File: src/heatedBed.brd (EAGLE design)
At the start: 100 x 100 mm, 20 parts, among them P2 LONG_PAD

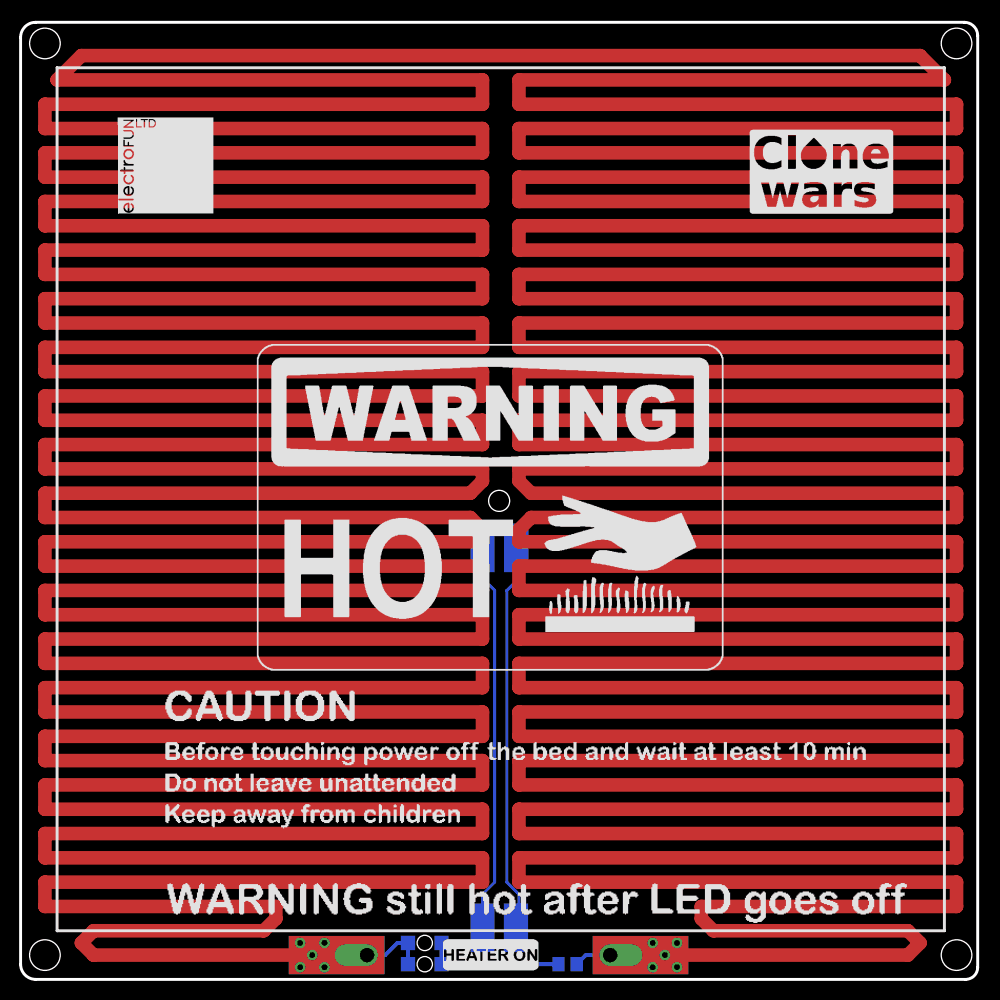
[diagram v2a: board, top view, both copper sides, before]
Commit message: Added board dimensions and modified drill sizes.
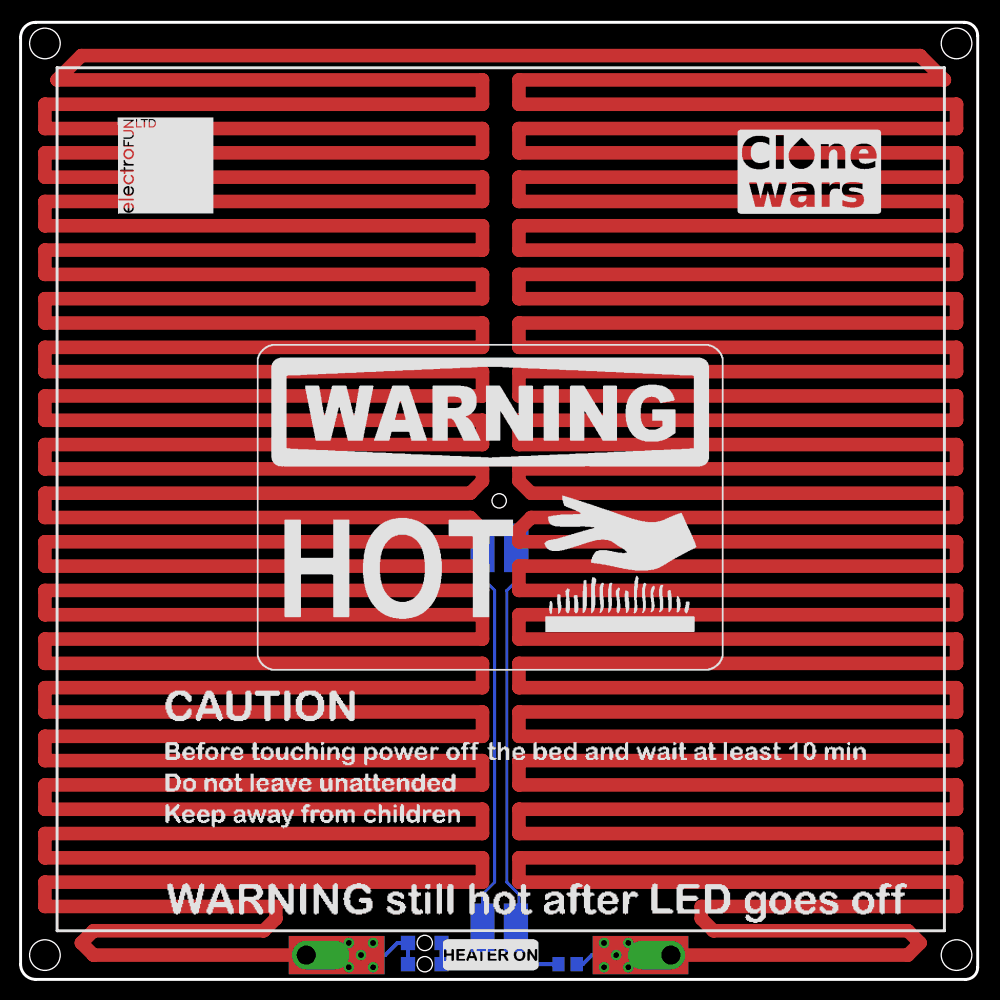
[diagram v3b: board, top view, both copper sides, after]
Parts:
- moved U$11 2.54 mm to (88.9, 58.7)
- moved U$3 1.27 mm to (74.9, 80.0)
- turned P2 to 0 degrees
- turned U$2 to 180 degrees
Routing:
- net P1: track 3547.0 -> 3543.8 mm
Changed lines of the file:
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@@
 <layer number="23" name="tOrigins" color="15" fill="1" visible="yes" active="yes"/>
 <layer number="24" name="bOrigins" color="15" fill="1" visible="yes" active="yes"/>
-<layer number="25" name="tNames" color="7" fill="1" visible="no" active="yes"/>
+<layer number="25" name="tNames" color="7" fill="1" visible="yes" active="yes"/>
 <layer number="26" name="bNames" color="7" fill="1" visible="yes" active="yes"/>
 <layer number="27" name="tValues" color="7" fill="1" visible="no" active="yes"/>
@@
 <layer number="45" name="Holes" color="7" fill="1" visible="yes" active="yes"/>
 <layer number="46" name="Milling" color="3" fill="1" visible="no" active="yes"/>
-<layer number="47" name="Measures" color="7" fill="1" visible="no" active="yes"/>
+<layer number="47" name="Measures" color="7" fill="1" visible="yes" active="yes"/>
 <layer number="48" name="Document" color="7" fill="1" visible="no" active="yes"/>
 <layer number="49" name="Reference" color="7" fill="1" visible="no" active="yes"/>
@@
 <wire x1="98.59685625" y1="100" x2="1.577515625" y2="100" width="0.3048" layer="20"/>
 <wire x1="1.577515625" y1="100" x2="0" y2="98.422484375" width="0.3048" layer="20" curve="90"/>
-<hole x="50" y="50" drill="2.2"/>
+<hole x="50" y="50" drill="1.5"/>
 <hole x="97.79" y="2.54" drill="3.2"/>
 <hole x="2.54" y="2.54" drill="3.2"/>
@@
 <wire x1="96.52" y1="5.08" x2="3.81" y2="5.08" width="0.3048" layer="21"/>
 <wire x1="3.81" y1="5.08" x2="3.81" y2="95.25" width="0.3048" layer="21"/>
+<dimension x1="2.54" y1="2.54" x2="97.79" y2="2.54" x3="50.165" y3="-5.08" textsize="1.778" layer="47" dtype="horizontal"/>
+<dimension x1="97.79" y1="2.54" x2="97.79" y2="97.79" x3="105.41" y3="50.165" textsize="1.778" layer="47" dtype="vertical"/>
+<dimension x1="0" y1="98.422484375" x2="100.0125" y2="81.28" x3="50.00625" y3="102.87" textsize="1.778" layer="47" dtype="horizontal"/>
+<dimension x1="1.577515625" y1="100" x2="8.89" y2="0" x3="-3.81" y3="50" textsize="1.778" layer="47" dtype="vertical"/>
 </plain>
 <attributes>
@@
 <attribute name="VALUE" x="56.515" y="4.1275" size="1.27" layer="28" rot="MR180"/>
 </element>
-<element name="U$2" library="fmc" package="LONG_PAD" value="LONG_PAD" x="33.02" y="2.54"/>
-<element name="P2" library="fmc" package="LONG_PAD" value="LONG_PAD" x="64.77" y="2.54" rot="R180"/>
+<element name="U$2" library="fmc" package="LONG_PAD" value="LONG_PAD" x="33.02" y="2.54" rot="R180"/>
+<element name="P2" library="fmc" package="LONG_PAD" value="LONG_PAD" x="64.77" y="2.54"/>
 <element name="PAD1" library="wirepad" package="SMD2,54-5,08" value="" x="51.8" y="45.085" smashed="yes" rot="MR0">
 <attribute name="VALUE" x="51.8" y="45.085" size="0.0254" layer="28" rot="MR0"/>
@@
 <element name="U$10" library="fmc" package="WARNING_HOT" value="" x="24.13" y="31.75"/>
 <element name="U$1" library="fmc" package="CAUTION" value="" x="13.97" y="2.54"/>
-<element name="U$11" library="fmc" package="ELECTROFUN_20X20" value="" x="88.9" y="61.2775" rot="MR0"/>
+<element name="U$11" library="fmc" package="ELECTROFUN_20X20" value="" x="88.9" y="58.7375" rot="MR0"/>
 <element name="U$12" library="fmc" package="ELECTROFUN_10X10" value="" x="10.16" y="80.01"/>
 <element name="U$8" library="fmc" package="BOARD_REF" value="" x="36.195" y="68.2625" rot="MR0"/>
-<element name="U$3" library="fmc" package="CLONE_WARS" value="" x="76.2" y="80.01"/>
+<element name="U$3" library="fmc" package="CLONE_WARS" value="" x="74.93" y="80.01"/>
 <element name="U$9" library="fmc" package="HEATERON" value="" x="44.1325" y="0.9525"/>
 </elements>
@@
 <contactref element="U$2" pad="P$1"/>
 <contactref element="L1" pad="C"/>
-<wire x1="64.77" y1="2.54" x2="61.595" y2="2.54" width="1.4224" layer="1"/>
-<wire x1="61.595" y1="2.54" x2="92.71" y2="2.54" width="1.4224" layer="1"/>
+<wire x1="64.77" y1="2.54" x2="67.945" y2="2.54" width="1.4224" layer="1"/>
 <wire x1="92.71" y1="2.54" x2="93.98" y2="3.81" width="1.4224" layer="1"/>
 <wire x1="93.98" y1="3.81" x2="92.71" y2="5.08" width="1.4224" layer="1"/>
@@
 <wire x1="7.62" y1="5.08" x2="6.35" y2="3.81" width="1.4224" layer="1"/>
 <wire x1="6.35" y1="3.81" x2="7.62" y2="2.54" width="1.4224" layer="1"/>
-<wire x1="7.62" y1="2.54" x2="33.02" y2="2.54" width="1.4224" layer="1"/>
 <contactref element="U$2" pad="P$2"/>
 <contactref element="U$2" pad="P$3"/>
 <contactref element="P2" pad="P$2"/>
 <contactref element="P2" pad="P$3"/>
-<wire x1="36.195" y1="2.54" x2="33.02" y2="2.54" width="0.4064" layer="1"/>
-<via x="29.21" y="3.81" extent="1-16" drill="0.6"/>
-<via x="29.21" y="1.27" extent="1-16" drill="0.6"/>
-<via x="30.48" y="2.54" extent="1-16" drill="0.6"/>
-<via x="31.75" y="3.81" extent="1-16" drill="0.6"/>
-<via x="31.75" y="1.27" extent="1-16" drill="0.6"/>
-<via x="66.04" y="3.81" extent="1-16" drill="0.6"/>
-<via x="68.58" y="3.81" extent="1-16" drill="0.6"/>
-<via x="67.31" y="2.54" extent="1-16" drill="0.6"/>
-<via x="66.04" y="1.27" extent="1-16" drill="0.6"/>
-<via x="68.58" y="1.27" extent="1-16" drill="0.6"/>
+<wire x1="29.845" y1="2.54" x2="33.02" y2="2.54" width="0.4064" layer="1"/>
+<via x="34.29" y="3.81" extent="1-16" drill="0.6"/>
 <wire x1="48.26" y1="45.72" x2="48.26" y2="46.99" width="1.4224" layer="1"/>
 <wire x1="48.26" y1="46.99" x2="46.99" y2="48.26" width="1.4224" layer="1"/>
@@
 <wire x1="53.34" y1="48.26" x2="52.07" y2="46.99" width="1.4224" layer="1"/>
 <wire x1="52.07" y1="46.99" x2="52.07" y2="45.72" width="1.4224" layer="1"/>
-<wire x1="61.595" y1="2.54" x2="59.0525" y2="2.54" width="0.4064" layer="16"/>
-<wire x1="59.0525" y1="2.54" x2="58.1" y2="1.5875" width="0.4064" layer="16"/>
 <wire x1="40.4775" y1="3.81" x2="40.64" y2="3.81" width="0.4064" layer="16"/>
-<wire x1="40.4775" y1="3.81" x2="39.37" y2="3.81" width="0.4064" layer="16"/>
-<wire x1="39.37" y1="3.81" x2="38.1" y2="2.54" width="0.4064" layer="16"/>
-<wire x1="38.1" y1="2.54" x2="36.195" y2="2.54" width="0.4064" layer="16"/>
 <wire x1="40.4775" y1="3.81" x2="40.4775" y2="1.5875" width="0.4064" layer="16"/>
 <wire x1="26.67" y1="7.62" x2="26.67" y2="6.35" width="1.4224" layer="1"/>
@@
 <wire x1="71.12" y1="6.35" x2="72.39" y2="5.08" width="1.4224" layer="1"/>
 <wire x1="72.39" y1="5.08" x2="92.71" y2="5.08" width="1.4224" layer="1"/>
-<wire x1="67.31" y1="2.54" x2="68.58" y2="3.81" width="0" layer="19" extent="1-1"/>
-<wire x1="66.04" y1="3.81" x2="67.31" y2="2.54" width="0" layer="19" extent="1-1"/>
-<wire x1="68.58" y1="1.27" x2="67.31" y2="2.54" width="0" layer="19" extent="1-1"/>
-<wire x1="64.77" y1="2.54" x2="66.04" y2="3.81" width="0" layer="19" extent="16-16"/>
+<wire x1="67.945" y1="2.54" x2="92.71" y2="2.54" width="1.4224" layer="1"/>
+<wire x1="29.845" y1="2.54" x2="7.62" y2="2.54" width="1.4224" layer="1"/>
+<wire x1="40.4775" y1="3.81" x2="39.37" y2="3.81" width="0.4064" layer="16"/>
+<wire x1="39.37" y1="3.81" x2="38.1" y2="2.54" width="0.4064" layer="16"/>
+<wire x1="38.1" y1="2.54" x2="33.02" y2="2.54" width="0.4064" layer="16"/>
+<wire x1="58.1" y1="1.5875" x2="58.7375" y2="1.5875" width="0.4064" layer="16"/>
+<wire x1="58.7375" y1="1.5875" x2="59.69" y2="2.54" width="0.4064" layer="16"/>
+<wire x1="59.69" y1="2.54" x2="64.77" y2="2.54" width="0.4064" layer="16"/>
+<via x="35.56" y="2.54" extent="1-16" drill="0.6"/>
+<via x="36.83" y="3.81" extent="1-16" drill="0.6"/>
+<via x="36.83" y="1.27" extent="1-16" drill="0.6"/>
+<via x="34.29" y="1.27" extent="1-16" drill="0.6"/>
+<via x="60.96" y="3.81" extent="1-16" drill="0.6"/>
+<via x="63.5" y="3.81" extent="1-16" drill="0.6"/>
+<via x="62.23" y="2.54" extent="1-16" drill="0.6"/>
+<via x="60.96" y="1.27" extent="1-16" drill="0.6"/>
+<via x="63.5" y="1.27" extent="1-16" drill="0.6"/>
+<wire x1="62.23" y1="2.54" x2="63.5" y2="3.81" width="0" layer="19" extent="1-1"/>
+<wire x1="60.96" y1="3.81" x2="62.23" y2="2.54" width="0" layer="19" extent="1-1"/>
+<wire x1="63.5" y1="1.27" x2="62.23" y2="2.54" width="0" layer="19" extent="1-1"/>
+<wire x1="60.96" y1="1.27" x2="62.23" y2="2.54" width="0" layer="19" extent="1-1"/>
+<wire x1="64.77" y1="2.54" x2="63.5" y2="3.81" width="0" layer="19" extent="16-16"/>
 <wire x1="64.77" y1="2.54" x2="64.77" y2="2.54" width="0" layer="19" extent="1-16"/>
 <wire x1="33.02" y1="2.54" x2="33.02" y2="2.54" width="0" layer="19" extent="1-16"/>
-<wire x1="66.04" y1="1.27" x2="67.31" y2="2.54" width="0" layer="19" extent="1-1"/>
-<wire x1="31.75" y1="3.81" x2="33.02" y2="2.54" width="0" layer="19" extent="1-1"/>
-<wire x1="30.48" y1="2.54" x2="31.75" y2="3.81" width="0" layer="19" extent="1-1"/>
-<wire x1="29.21" y1="3.81" x2="30.48" y2="2.54" width="0" layer="19" extent="1-1"/>
-<wire x1="31.75" y1="1.27" x2="33.02" y2="2.54" width="0" layer="19" extent="1-1"/>
-<wire x1="29.21" y1="1.27" x2="30.48" y2="2.54" width="0" layer="19" extent="1-1"/>
+<wire x1="36.83" y1="3.81" x2="38.1" y2="2.54" width="0" layer="19" extent="16-16"/>
+<wire x1="35.56" y1="2.54" x2="36.83" y2="3.81" width="0" layer="19" extent="1-1"/>
+<wire x1="34.29" y1="3.81" x2="33.02" y2="2.54" width="0" layer="19" extent="1-1"/>
+<wire x1="36.83" y1="1.27" x2="38.1" y2="2.54" width="0" layer="19" extent="16-16"/>
+<wire x1="34.29" y1="1.27" x2="33.02" y2="2.54" width="0" layer="19" extent="1-1"/>
 </signal>
 <signal name="N$4">

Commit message: Prepare Rev B release.
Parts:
- moved R1 0.95 mm to (56.2, 1.59)
- moved L1 0.63 mm to (42.9, 3.81)
- moved L2 0.63 mm to (42.9, 1.59)
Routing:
- net P1: track 3543.8 -> 3545.7 mm
- net N$4: track 14.4 -> 12.9 mm
- added copper zone on layer 16, net N$1
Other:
- board text added: "B"
- board text added: "CERN OHL v1.2"
- board text removed: "A"

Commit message: Prepared for Rev B.
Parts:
- added R2: NTCS0805E3104FXT, rcl:R0805
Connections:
- net N$3: now also R2.2
- net N$5: now also R2.1
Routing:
- net N$5: track 40.7 -> 49.8 mm
- net N$3: track 42.0 -> 50.5 mm
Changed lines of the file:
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@@
 <setting verticaltext="up"/>
 </settings>
-<grid distance="0.05" unitdist="inch" unit="mm" style="dots" multiple="1" display="yes" altdistance="12.5" altunitdist="mil" altunit="mm"/>
+<grid distance="0.05" unitdist="inch" unit="mm" style="lines" multiple="1" display="yes" altdistance="6.25" altunitdist="mil" altunit="mm"/>
 <layers>
 <layer number="1" name="Top" color="4" fill="1" visible="yes" active="yes"/>
@@
 <layer number="20" name="Dimension" color="15" fill="1" visible="yes" active="yes"/>
 <layer number="21" name="tPlace" color="7" fill="1" visible="yes" active="yes"/>
-<layer number="22" name="bPlace" color="7" fill="1" visible="yes" active="yes"/>
-<layer number="23" name="tOrigins" color="15" fill="1" visible="no" active="yes"/>
-<layer number="24" name="bOrigins" color="15" fill="1" visible="yes" active="yes"/>
+<layer number="22" name="bPlace" color="7" fill="1" visible="no" active="yes"/>
+<layer number="23" name="tOrigins" color="15" fill="1" visible="yes" active="yes"/>
+<layer number="24" name="bOrigins" color="15" fill="1" visible="no" active="yes"/>
 <layer number="25" name="tNames" color="7" fill="1" visible="yes" active="yes"/>
-<layer number="26" name="bNames" color="7" fill="1" visible="yes" active="yes"/>
+<layer number="26" name="bNames" color="7" fill="1" visible="no" active="yes"/>
 <layer number="27" name="tValues" color="7" fill="1" visible="no" active="yes"/>
 <layer number="28" name="bValues" color="7" fill="1" visible="no" active="yes"/>
@@
 <layer number="43" name="vRestrict" color="2" fill="10" visible="no" active="yes"/>
 <layer number="44" name="Drills" color="7" fill="1" visible="no" active="yes"/>
-<layer number="45" name="Holes" color="7" fill="1" visible="yes" active="yes"/>
+<layer number="45" name="Holes" color="7" fill="1" visible="no" active="yes"/>
 <layer number="46" name="Milling" color="3" fill="1" visible="no" active="yes"/>
 <layer number="47" name="Measures" color="7" fill="1" visible="no" active="yes"/>
@@
 <elements>
 <element name="L1" library="led" package="CHIPLED_1206_REVERSE" value="597-6001-607F" x="42.8625" y="3.81" smashed="yes" rot="MR270">
-<attribute name="NAME" x="38.4175" y="4.445" size="1" layer="26" ratio="12" rot="MR180"/>
+<attribute name="NAME" x="38.4175" y="4.445" size="1" layer="26" font="vector" ratio="12" rot="MR180"/>
 <attribute name="VALUE" x="44.1325" y="1.27" size="1.27" layer="28" rot="MR0"/>
 </element>
 <element name="L2" library="led" package="CHIPLED_1206_REVERSE" value="" x="42.8625" y="1.5875" smashed="yes" rot="MR90">
-<attribute name="NAME" x="38.4175" y="2.2225" size="1.016" layer="26" ratio="12" rot="MR180"/>
+<attribute name="NAME" x="38.4175" y="2.2225" size="1.016" layer="26" font="vector" ratio="12" rot="MR180"/>
 <attribute name="VALUE" x="41.5925" y="4.1275" size="1.27" layer="28" rot="MR180"/>
 </element>
 <element name="R1" library="rcl" package="R0805" value="2K2" x="56.1975" y="1.5875" smashed="yes" rot="MR180">
-<attribute name="NAME" x="55.245" y="3.4925" size="0.8128" layer="26" ratio="12" rot="MR180"/>
+<attribute name="NAME" x="55.245" y="3.4925" size="0.8128" layer="26" font="vector" ratio="12" rot="MR180"/>
 <attribute name="VALUE" x="55.5625" y="4.1275" size="1.27" layer="28" rot="MR180"/>
 </element>
@@
 <element name="U$3" library="fmc" package="CLONE_WARS" value="" x="74.93" y="80.01"/>
 <element name="U$9" library="fmc" package="HEATERON" value="" x="44.1325" y="0.9525"/>
+<element name="R2" library="rcl" package="R0805" value="NTCS0805E3104FXT" x="50" y="52.86375" smashed="yes" rot="MR180">
+<attribute name="NAME" x="49.20625" y="55.08625" size="0.8128" layer="26" font="vector" ratio="12" rot="MR180"/>
+<attribute name="VALUE" x="49.365" y="55.40375" size="1.27" layer="28" rot="MR180"/>
+</element>
 </elements>
 <signals>
@@
 <wire x1="52.07" y1="44.815" x2="52.07" y2="41.91" width="0.3048" layer="16"/>
 <wire x1="52.07" y1="41.91" x2="50.8" y2="40.64" width="0.3048" layer="16"/>
+<contactref element="R2" pad="2"/>
+<wire x1="51.8" y1="45.45" x2="51.8" y2="48.3075" width="0.3048" layer="16"/>
+<wire x1="51.8" y1="48.3075" x2="52.705" y2="49.2125" width="0.3048" layer="16"/>
+<wire x1="52.705" y1="49.2125" x2="52.705" y2="51.10875" width="0.3048" layer="16"/>
+<wire x1="52.705" y1="51.10875" x2="50.95" y2="52.86375" width="0.3048" layer="16"/>
 </signal>
 <signal name="N$5">
@@
 <wire x1="49.53" y1="40.64" x2="48.26" y2="41.91" width="0.3048" layer="16"/>
 <wire x1="48.26" y1="41.91" x2="48.26" y2="45.085" width="0.3048" layer="16"/>
+<contactref element="R2" pad="1"/>
+<wire x1="48.26" y1="45.085" x2="48.26" y2="48.10125" width="0.3048" layer="16"/>
+<wire x1="48.26" y1="48.10125" x2="47.14875" y2="49.2125" width="0.3048" layer="16"/>
+<wire x1="47.14875" y1="49.2125" x2="47.14875" y2="50.9625" width="0.3048" layer="16"/>
+<wire x1="47.14875" y1="50.9625" x2="49.05" y2="52.86375" width="0.3048" layer="16"/>
 </signal>
 <signal name="N$1">

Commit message: Updated revision B files.
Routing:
- net P1: vias 10 -> 16
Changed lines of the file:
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@@
 <?xml version="1.0" encoding="utf-8"?>
 <!DOCTYPE eagle SYSTEM "eagle.dtd">
-<eagle version="7.4.0">
+<eagle version="7.0.0">
 <drawing>
 <settings>
@@
 <layers>
 <layer number="1" name="Top" color="4" fill="1" visible="yes" active="yes"/>
-<layer number="16" name="Bottom" color="1" fill="1" visible="yes" active="yes"/>
+<layer number="16" name="Bottom" color="1" fill="1" visible="no" active="yes"/>
 <layer number="17" name="Pads" color="2" fill="1" visible="yes" active="yes"/>
 <layer number="18" name="Vias" color="2" fill="1" visible="yes" active="yes"/>
@@
 <via x="60.96" y="1.27" extent="1-16" drill="0.6"/>
 <via x="63.5" y="1.27" extent="1-16" drill="0.6"/>
+<via x="33.02" y="2.54" extent="1-16" drill="0.6"/>
+<via x="31.75" y="3.81" extent="1-16" drill="0.6"/>
+<via x="31.75" y="1.27" extent="1-16" drill="0.6"/>
+<via x="64.77" y="2.54" extent="1-16" drill="0.6"/>
+<via x="66.04" y="3.81" extent="1-16" drill="0.6"/>
+<via x="66.04" y="1.27" extent="1-16" drill="0.6"/>
+<wire x1="64.77" y1="2.54" x2="66.04" y2="3.81" width="0" layer="19" extent="16-16"/>
+<wire x1="63.5" y1="3.81" x2="64.77" y2="2.54" width="0" layer="19" extent="16-16"/>
+<wire x1="66.04" y1="1.27" x2="64.77" y2="2.54" width="0" layer="19" extent="16-16"/>
+<wire x1="60.96" y1="3.81" x2="59.69" y2="2.54" width="0" layer="19" extent="16-16"/>
 <wire x1="62.23" y1="2.54" x2="63.5" y2="3.81" width="0" layer="19" extent="1-1"/>
-<wire x1="60.96" y1="3.81" x2="62.23" y2="2.54" width="0" layer="19" extent="1-1"/>
-<wire x1="63.5" y1="1.27" x2="62.23" y2="2.54" width="0" layer="19" extent="1-1"/>
-<wire x1="60.96" y1="1.27" x2="62.23" y2="2.54" width="0" layer="19" extent="1-1"/>
-<wire x1="64.77" y1="2.54" x2="63.5" y2="3.81" width="0" layer="19" extent="16-16"/>
-<wire x1="64.77" y1="2.54" x2="64.77" y2="2.54" width="0" layer="19" extent="1-16"/>
-<wire x1="33.02" y1="2.54" x2="33.02" y2="2.54" width="0" layer="19" extent="1-16"/>
+<wire x1="63.5" y1="1.27" x2="64.77" y2="2.54" width="0" layer="19" extent="16-16"/>
+<wire x1="60.96" y1="1.27" x2="59.69" y2="2.54" width="0" layer="19" extent="16-16"/>
 <wire x1="36.83" y1="3.81" x2="38.1" y2="2.54" width="0" layer="19" extent="16-16"/>
 <wire x1="35.56" y1="2.54" x2="36.83" y2="3.81" width="0" layer="19" extent="1-1"/>
-<wire x1="34.29" y1="3.81" x2="33.02" y2="2.54" width="0" layer="19" extent="1-1"/>
+<wire x1="34.29" y1="3.81" x2="33.02" y2="2.54" width="0" layer="19" extent="16-16"/>
 <wire x1="36.83" y1="1.27" x2="38.1" y2="2.54" width="0" layer="19" extent="16-16"/>
-<wire x1="34.29" y1="1.27" x2="33.02" y2="2.54" width="0" layer="19" extent="1-1"/>
+<wire x1="34.29" y1="1.27" x2="33.02" y2="2.54" width="0" layer="19" extent="16-16"/>
+<wire x1="31.75" y1="3.81" x2="33.02" y2="2.54" width="0" layer="19" extent="16-16"/>
+<wire x1="31.75" y1="1.27" x2="33.02" y2="2.54" width="0" layer="19" extent="16-16"/>
 </signal>
 <signal name="N$4">
